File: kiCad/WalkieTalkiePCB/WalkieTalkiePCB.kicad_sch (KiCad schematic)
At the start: 21 parts, among them SW1 UP, SW2 DWN, SW3 MODE, SW4 TLK, SW5 XTRA, U1 I2S-MIC, U2 3006-ADA_Adafruit_, U3 WROOM-32_DEVKITV1, U4 OLED_DISPLAY, U5 BAT-C-10TYPEC, U6 PSM-301, U7 PBS-LED-1606WH-L

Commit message: Kicad Finalized Schematic
Colin Jack is smort
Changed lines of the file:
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@@
   (junction (at 120.65 54.61) (diameter 0) (color 0 0 0 0)
-  )
-  (junction (at 87.63 87.63) (diameter 0) (color 0 0 0 0)
   )
   (junction (at 120.65 68.58) (diameter 0) (color 0 0 0 0)
@@
     (stroke (width 0) (type default) (color 0 0 0 0))
   )
-  (wire (pts (xy 87.63 87.63) (xy 87.63 107.95))
-    (stroke (width 0) (type default) (color 0 0 0 0))
-  )
   (wire (pts (xy 64.77 124.46) (xy 86.36 124.46))
     (stroke (width 0) (type default) (color 0 0 0 0))
@@
     (stroke (width 0) (type default) (color 0 0 0 0))
   )
-  (wire (pts (xy 87.63 87.63) (xy 97.79 87.63))
-    (stroke (width 0) (type default) (color 0 0 0 0))
-  )
   (wire (pts (xy 217.17 124.46) (xy 217.17 133.35))
     (stroke (width 0) (type default) (color 0 0 0 0))
@@
     (stroke (width 0) (type default) (color 0 0 0 0))
   )
-  (wire (pts (xy 87.63 107.95) (xy 113.03 107.95))
-    (stroke (width 0) (type default) (color 0 0 0 0))
-  )
   (wire (pts (xy 210.82 107.95) (xy 210.82 121.92))
     (stroke (width 0) (type default) (color 0 0 0 0))
@@
     (stroke (width 0) (type default) (color 0 0 0 0))
   )
-  (wire (pts (xy 86.36 87.63) (xy 87.63 87.63))
+  (wire (pts (xy 86.36 87.63) (xy 97.79 87.63))
     (stroke (width 0) (type default) (color 0 0 0 0))
   )
@@
     (pin "1")
   )
-  (symbol (lib_id "power:PWR_FLAG") (at 30.48 19.05 180) (unit 1)
-    (in_bom yes) (on_board yes) (fields_autoplaced)
-    (property "Reference" "#FLG0102" (id 0) (at 30.48 20.955 0)
-      (effects (font (size 1.27 1.27)) hide)
-    )
-    (property "Value" "PWR_FLAG" (id 1) (at 30.48 24.13 0))
-    (property "Footprint" "" (id 2) (at 30.48 19.05 0)
-      (effects (font (size 1.27 1.27)) hide)
-    )
-    (property "Datasheet" "~" (id 3) (at 30.48 19.05 0)
-      (effects (font (size 1.27 1.27)) hide)
-    )
-    (pin "1")
-  )
   (symbol (lib_id "power:VCC") (at 264.16 93.98 0) (unit 1)
     (in_bom yes) (on_board yes) (fields_autoplaced)
@@
     (pin "2")
   )
-  (symbol (lib_id "power:VCC") (at 20.32 19.05 0) (unit 1)
-    (in_bom yes) (on_board yes) (fields_autoplaced)
-    (property "Reference" "#PWR0102" (id 0) (at 20.32 22.86 0)
-      (effects (font (size 1.27 1.27)) hide)
-    )
-    (property "Value" "VCC" (id 1) (at 20.32 13.97 0))
-    (property "Footprint" "" (id 2) (at 20.32 19.05 0)
-      (effects (font (size 1.27 1.27)) hide)
-    )
-    (property "Datasheet" "" (id 3) (at 20.32 19.05 0)
-      (effects (font (size 1.27 1.27)) hide)
-    )
-    (pin "1")
-  )
   (symbol (lib_id "Device:R") (at 199.39 116.84 0) (unit 1)
     (in_bom yes) (on_board yes) (fields_autoplaced)
@@
     (pin "1")
     (pin "2")
-  )
-  (symbol (lib_id "power:GND") (at 30.48 19.05 180) (unit 1)
-    (in_bom yes) (on_board yes) (fields_autoplaced)
-    (property "Reference" "#PWR0101" (id 0) (at 30.48 12.7 0)
-      (effects (font (size 1.27 1.27)) hide)
-    )
-    (property "Value" "GND" (id 1) (at 30.48 13.97 0))
-    (property "Footprint" "" (id 2) (at 30.48 19.05 0)
-      (effects (font (size 1.27 1.27)) hide)
-    )
-    (property "Datasheet" "" (id 3) (at 30.48 19.05 0)
-      (effects (font (size 1.27 1.27)) hide)
-    )
-    (pin "1")
   )
   (symbol (lib_id "Device:Speaker") (at 121.92 157.48 270) (unit 1)
@@
     (pin "2")
   )
-  (symbol (lib_id "power:PWR_FLAG") (at 20.32 19.05 180) (unit 1)
-    (in_bom yes) (on_board yes) (fields_autoplaced)
-    (property "Reference" "#FLG0103" (id 0) (at 20.32 20.955 0)
-      (effects (font (size 1.27 1.27)) hide)
-    )
-    (property "Value" "PWR_FLAG" (id 1) (at 20.32 24.13 0))
-    (property "Footprint" "" (id 2) (at 20.32 19.05 0)
-      (effects (font (size 1.27 1.27)) hide)
-    )
-    (property "Datasheet" "~" (id 3) (at 20.32 19.05 0)
-      (effects (font (size 1.27 1.27)) hide)
-    )
-    (pin "1")
-  )
   (symbol (lib_id "power:VCC") (at 158.75 127 180) (unit 1)
     (in_bom yes) (on_board yes) (fields_autoplaced)
@@
       (reference "#FLG0101") (unit 1) (value "PWR_FLAG") (footprint "")
     )
-    (path "/11edab21-699f-42c5-8fca-4d804925d8d4"
-      (reference "#FLG0102") (unit 1) (value "PWR_FLAG") (footprint "")
-    )
-    (path "/f00c2272-6d64-46d9-8dbf-cbfe852eec09"
-      (reference "#FLG0103") (unit 1) (value "PWR_FLAG") (footprint "")
-    )
     (path "/dde1a039-bfd3-47af-b1ef-c50a0b5b415b"
       (reference "#FLG0104") (unit 1) (value "PWR_FLAG") (footprint "")
     )
-    (path "/6ede4dce-002e-42b0-be72-ae433793c82f"
-      (reference "#PWR0101") (unit 1) (value "GND") (footprint "")
-    )
-    (path "/1ae2b874-5753-46d5-b3c2-00fc7ac6cbb4"
-      (reference "#PWR0102") (unit 1) (value "VCC") (footprint "")
-    )
     (path "/1229cc48-894a-4616-bade-a8d099b6e899"

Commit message: PCB
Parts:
- BT1: footprint (none) -> ESP32 Walkie-Talkie:Battery-Contacts
- LS1: footprint (none) -> ESP32 Walkie-Talkie:Speaker
- U1: footprint (none) -> ESP32 Walkie-Talkie:I2S-Mic
- U2: footprint (none) -> ESP32 Walkie-Talkie:Amplifier
- U5: footprint (none) -> ESP32 Walkie-Talkie:USBC-BMS
- U6: footprint (none) -> ESP32 Walkie-Talkie:Voltage-Regulator
- U7: footprint (none) -> ESP32 Walkie-Talkie:PBS-Button
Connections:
- net at U6.VIN+: now also U5.V+ (VOUT); no longer U5.v+ (VOUT)
- net at U6.VIN-: now also U5.V- (VOUT); no longer U5.v- (VOUT)
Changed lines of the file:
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@@
     (property "Reference" "U1" (id 0) (at 71.12 125.73 0))
     (property "Value" "I2S-MIC" (id 1) (at 71.12 128.27 0))
-    (property "Footprint" "" (id 2) (at 71.12 139.7 0)
+    (property "Footprint" "ESP32 Walkie-Talkie:I2S-Mic" (id 2) (at 71.12 139.7 0)
       (effects (font (size 1.27 1.27)) hide)
     )
@@
       (effects (font (size 1.27 1.27)) (justify left))
     )
-    (property "Footprint" "" (id 2) (at 125.73 125.73 0)
+    (property "Footprint" "ESP32 Walkie-Talkie:Amplifier" (id 2) (at 125.73 125.73 0)
       (effects (font (size 1.27 1.27)) hide)
     )
@@
     (property "Reference" "BT1" (id 0) (at 214.122 127 90))
     (property "Value" "Battery_Cell" (id 1) (at 214.122 129.54 90))
-    (property "Footprint" "" (id 2) (at 213.614 134.62 90)
+    (property "Footprint" "ESP32 Walkie-Talkie:Battery-Contacts" (id 2) (at 213.614 134.62 90)
       (effects (font (size 1.27 1.27)) hide)
     )
@@
       (effects (font (size 1.27 1.27)) (justify left))
     )
-    (property "Footprint" "" (id 2) (at 116.84 157.48 0)
+    (property "Footprint" "ESP32 Walkie-Talkie:Speaker" (id 2) (at 116.84 157.48 0)
       (effects (font (size 1.27 1.27)) hide)
     )
@@
       (effects (font (size 1.27 1.27)) (justify left))
     )
-    (property "Footprint" "" (id 2) (at 213.36 88.9 0)
+    (property "Footprint" "ESP32 Walkie-Talkie:USBC-BMS" (id 2) (at 213.36 88.9 0)
       (effects (font (size 1.27 1.27)) hide)
     )
@@
     (pin "B+")
     (pin "B-")
-    (pin "v+")
-    (pin "v-")
+    (pin "V+")
+    (pin "V-")
   )
   (symbol (lib_id "WalkieTalkie:PSM-301") (at 214.63 91.44 180) (unit 1)
@@
     (property "Reference" "U6" (id 0) (at 213.995 88.9 0))
     (property "Value" "PSM-301" (id 1) (at 213.995 91.44 0))
-    (property "Footprint" "" (id 2) (at 214.63 91.44 0)
+    (property "Footprint" "ESP32 Walkie-Talkie:Voltage-Regulator" (id 2) (at 214.63 91.44 0)
       (effects (font (size 1.27 1.27)) hide)
     )
@@
     (property "Reference" "U7" (id 0) (at 262.89 82.55 0))
     (property "Value" "PBS-LED-1606WH-L" (id 1) (at 262.89 85.09 0))
-    (property "Footprint" "" (id 2) (at 251.46 87.63 0)
+    (property "Footprint" "ESP32 Walkie-Talkie:PBS-Button" (id 2) (at 251.46 87.63 0)
       (effects (font (size 1.27 1.27)) hide)
     )
@@
     )
     (path "/565d06fb-9534-48e0-a256-9134feb87b03"
-      (reference "BT1") (unit 1) (value "Battery_Cell") (footprint "")
+      (reference "BT1") (unit 1) (value "Battery_Cell") (footprint "ESP32 Walkie-Talkie:Battery-Contacts")
     )
     (path "/729b3da4-0313-41c5-9118-f5a5d81e720a"
-      (reference "LS1") (unit 1) (value "Speaker") (footprint "")
+      (reference "LS1") (unit 1) (value "Speaker") (footprint "ESP32 Walkie-Talkie:Speaker")
     )
     (path "/e9eb94ed-4dc4-450e-8838-fce3918021eb"
@@
     )
     (path "/06189962-e377-4982-9780-d7fd696848a8"
-      (reference "U1") (unit 1) (value "I2S-MIC") (footprint "")
+      (reference "U1") (unit 1) (value "I2S-MIC") (footprint "ESP32 Walkie-Talkie:I2S-Mic")
     )
     (path "/0aeafca2-1eb3-4ed4-9136-be9da76bceb3"
-      (reference "U2") (unit 1) (value "3006-ADA_Adafruit_") (footprint "")
+      (reference "U2") (unit 1) (value "3006-ADA_Adafruit_") (footprint "ESP32 Walkie-Talkie:Amplifier")
     )
     (path "/c943f0b5-36cc-4140-b0cd-7d88893d98d2"
@@
     )
     (path "/742e5744-c81c-4950-88db-007b37fa2b34"
-      (reference "U5") (unit 1) (value "BAT-C-10TYPEC") (footprint "")
+      (reference "U5") (unit 1) (value "BAT-C-10TYPEC") (footprint "ESP32 Walkie-Talkie:USBC-BMS")
     )
     (path "/75cb9de8-b81e-4952-a80b-0fda81fc1740"
-      (reference "U6") (unit 1) (value "PSM-301") (footprint "")
+      (reference "U6") (unit 1) (value "PSM-301") (footprint "ESP32 Walkie-Talkie:Voltage-Regulator")
     )
     (path "/906709c3-3cb2-4376-82e4-c4c35bb617e0"
-      (reference "U7") (unit 1) (value "PBS-LED-1606WH-L") (footprint "")
-    )
-  )
+      (reference "U7") (unit 1) (value "PBS-LED-1606WH-L") (footprint "ESP32 Walkie-Talkie:PBS-Button")
+    )
+  )

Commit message: PCB
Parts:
- removed U1: I2S-MIC, ESP32 Walkie-Talkie:I2S-Mic, symbol WalkieTalkie:I2S-MIC
- removed U2: 3006-ADA_Adafruit_, ESP32 Walkie-Talkie:Amplifier, symbol WalkieTalkie:3006-ADA_Adafruit_
- removed U3: WROOM-32_DEVKITV1, symbol WROOM32-DEVKITV1:WROOM-32_DEVKITV1
- removed U4: OLED_DISPLAY, symbol WalkieTalkie:OLED_DISPLAY
- removed U5: BAT-C-10TYPEC, ESP32 Walkie-Talkie:USBC-BMS, symbol WalkieTalkie:BAT-C-10TYPEC
- removed U6: PSM-301, ESP32 Walkie-Talkie:Voltage-Regulator, symbol WalkieTalkie:PSM-301
- removed U7: PBS-LED-1606WH-L, ESP32 Walkie-Talkie:PBS-Button, symbol WalkieTalkie:PBS-LED-1606WH-L
- added U1: BAT-C-10TYPEC_(BMS), ESP32-Walkie-Talkie-Footprints-Remaster:BAT-C-10TYPEC-BMS, symbol Walkie-Talkie-Symbols-Remastered:BAT-C-10TYPEC_(BMS)
- added U2: PSM-301-Voltage-Regulator, ESP32-Walkie-Talkie-Footprints-Remaster:PSM-301-Voltage-Regulator, symbol Walkie-Talkie-Symbols-Remastered:PSM-301-Voltage-Regulator
- added U3: PBS-LED-1606WH-L_(Toggle_Button), ESP32-Walkie-Talkie-Footprints-Remaster:PBS-LED-1606WH-L-Toggle-Switch, symbol Walkie-Talkie-Symbols-Remastered:PBS-LED-1606WH-L_(Toggle_Button)
- added U4: I2S-128X64-OLED-LCD_, ESP32-Walkie-Talkie-Footprints-Remaster:I2S-128x64-OLED-LCD, symbol Walkie-Talkie-Symbols-Remastered:I2S-128X64-OLED-LCD_
- added U5: I2S-INMP441_(MIC), ESP32-Walkie-Talkie-Footprints-Remaster:I2SINMP441-MIC, symbol Walkie-Talkie-Symbols-Remastered:I2S-INMP441_(MIC)
- added U6: Amplifier, ESP32-Walkie-Talkie-Footprints-Remaster:Amplifier, symbol Walkie-Talkie-Symbols-Remastered:Amplifier
- added U7: ESP-WROOM-32, esp32_devkit_v1_doit:esp32_devkit_v1_doit, symbol Walkie-Talkie-Symbols-Remastered:ESP-WROOM-32
- BT1: footprint ESP32 Walkie-Talkie:Battery-Contacts -> ESP32-Walkie-Talkie-Footprints-Remaster:BATTERY-CONTACTS
- LS1: footprint ESP32 Walkie-Talkie:Speaker -> ESP32-Walkie-Talkie-Footprints-Remaster:SPEAKER
- R1, R2, R3, R4, R5: footprint (none) -> Resistor_THT:R_Axial_DIN0207_L6.3mm_D2.5mm_P10.16mm_Horizontal
- R6: value 2k2 -> 2K; footprint (none) -> Resistor_THT:R_Axial_DIN0207_L6.3mm_D2.5mm_P10.16mm_Horizontal
- R7: value 2k -> 2K2; footprint (none) -> Resistor_THT:R_Axial_DIN0207_L6.3mm_D2.5mm_P10.16mm_Horizontal
- SW1, SW2, SW3, SW4, SW5: footprint (none) -> ESP32-Walkie-Talkie-Footprints-Remaster:PUSH-BUTTON-CONTACTS
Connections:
- net GND: now also U2.2 (VOUT-), U3.2 (-), U4.2 (GND), U5.3 (L/R), U5.6 (GND), U6.4 (GAIN), U6.6 (GND)
- net VCC: now also U2.1 (VOUT+), U3.1 (+), U4.1 (VCC), U5.5 (VDD), U6.7 (VIN)
- net at LS1.1: now also U6.8 (-)
- net at LS1.2: now also U6.9 (+)
- net at R4.2, SW4.2: now also U7.10 (D27)
- net at R3.2, SW3.2: now also U7.9 (D26)
- net at R6.2, R7.1: now also U7.4 (D34)
- net at BT1.1 (+), R7.2: now also U1.2 (B+), U3.3 (CC)
- net at R1.2, SW1.2: now also U7.23 (D5)
- net at R2.2, SW2.2: now also U7.21 (D19)
- net at BT1.2 (-): now also U1.3 (B-)
- net at R5.2, SW5.2: now also U7.5 (D35)
- new net: U5.1 (SCK), U6.2 (BLCK), U7.6 (D32)
- new net: U5.2 (WS), U6.1 (LRC), U7.8 (D25)
- new net: U5.4 (SD), U7.7 (D33)
- new net: U2.5 (EN), U3.4 (NO)
- new net: U1.1 (OUT+), U2.4 (VIN+)
- new net: U1.4 (OUT-), U2.3 (VIN-)
- new net: U6.3 (DIN), U7.11 (D14)
- new net: U4.3 (SCL), U7.17 (D22)
- new net: U4.4 (SDA), U7.20 (D21)
- no-connect marks 20 -> 22
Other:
- note added: "Interact"
- note removed: "DISPLAY"
- note removed: "Input System"
- note removed: "Power Management"
- moved on the sheet: R1, R2, R3, R4, R5, SW1, SW2, SW3, SW4, SW5

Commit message: PCB
Why do we live. Just to suffer.
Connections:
- net GND: now also U7.29 (GND)
- net VCC: now also U7.30 (3V3)
- no-connect marks 22 -> 20
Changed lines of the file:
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@@
   (no_connect (at 207.01 87.63))
   (no_connect (at 165.1 96.52))
-  (no_connect (at 165.1 109.22))
   (no_connect (at 139.7 106.68))
   (no_connect (at 165.1 83.82))
@@
   (no_connect (at 139.7 78.74))
   (no_connect (at 165.1 76.2))
-  (no_connect (at 165.1 111.76))
   (no_connect (at 139.7 111.76))
   (no_connect (at 165.1 99.06))
@@
     (stroke (width 0) (type default) (color 0 0 0 0))
   )
+  (wire (pts (xy 165.1 111.76) (xy 165.1 115.57))
+    (stroke (width 0) (type default) (color 0 0 0 0))
+  )
   (wire (pts (xy 212.09 114.3) (xy 212.09 85.09))
     (stroke (width 0) (type default) (color 0 0 0 0))
@@
     (stroke (width 0) (type default) (color 0 0 0 0))
   )
+  (wire (pts (xy 168.91 109.22) (xy 168.91 113.03))
+    (stroke (width 0) (type default) (color 0 0 0 0))
+  )
   (wire (pts (xy 134.62 123.19) (xy 134.62 128.27))
     (stroke (width 0) (type default) (color 0 0 0 0))
@@
   )
   (wire (pts (xy 91.44 147.32) (xy 91.44 148.59))
+    (stroke (width 0) (type default) (color 0 0 0 0))
+  )
+  (wire (pts (xy 165.1 109.22) (xy 168.91 109.22))
     (stroke (width 0) (type default) (color 0 0 0 0))
   )
@@
     (pin "1")
     (pin "2")
+  )
+  (symbol (lib_id "power:GND") (at 168.91 113.03 0) (unit 1)
+    (in_bom yes) (on_board yes) (fields_autoplaced)
+    (property "Reference" "#PWR011" (id 0) (at 168.91 119.38 0)
+      (effects (font (size 1.27 1.27)) hide)
+    )
+    (property "Value" "GND" (id 1) (at 168.91 118.11 0))
+    (property "Footprint" "" (id 2) (at 168.91 113.03 0)
+      (effects (font (size 1.27 1.27)) hide)
+    )
+    (property "Datasheet" "" (id 3) (at 168.91 113.03 0)
+      (effects (font (size 1.27 1.27)) hide)
+    )
+    (pin "1")
   )
   (symbol (lib_id "Switch:SW_Push") (at 83.82 76.2 90) (unit 1)
@@
     (pin "4")
     (pin "5")
+  )
+  (symbol (lib_id "power:VCC") (at 165.1 115.57 180) (unit 1)
+    (in_bom yes) (on_board yes) (fields_autoplaced)
+    (property "Reference" "#PWR010" (id 0) (at 165.1 111.76 0)
+      (effects (font (size 1.27 1.27)) hide)
+    )
+    (property "Value" "VCC" (id 1) (at 165.1 120.65 0))
+    (property "Footprint" "" (id 2) (at 165.1 115.57 0)
+      (effects (font (size 1.27 1.27)) hide)
+    )
+    (property "Datasheet" "" (id 3) (at 165.1 115.57 0)
+      (effects (font (size 1.27 1.27)) hide)
+    )
+    (pin "1")
   )
   (symbol (lib_id "Walkie-Talkie-Symbols-Remastered:BAT-C-10TYPEC_(BMS)") (at 203.2 97.79 180) (unit 1)
@@
       (reference "#PWR09") (unit 1) (value "VCC") (footprint "")
     )
+    (path "/91b2fa62-6d51-424a-b6bc-28f3d4391629"
+      (reference "#PWR010") (unit 1) (value "VCC") (footprint "")
+    )
+    (path "/4c787647-1296-428b-8dc3-b9558523d840"
+      (reference "#PWR011") (unit 1) (value "GND") (footprint "")
+    )
     (path "/52a0511d-0ae3-46a1-aba7-f13cd3fb2bd9"

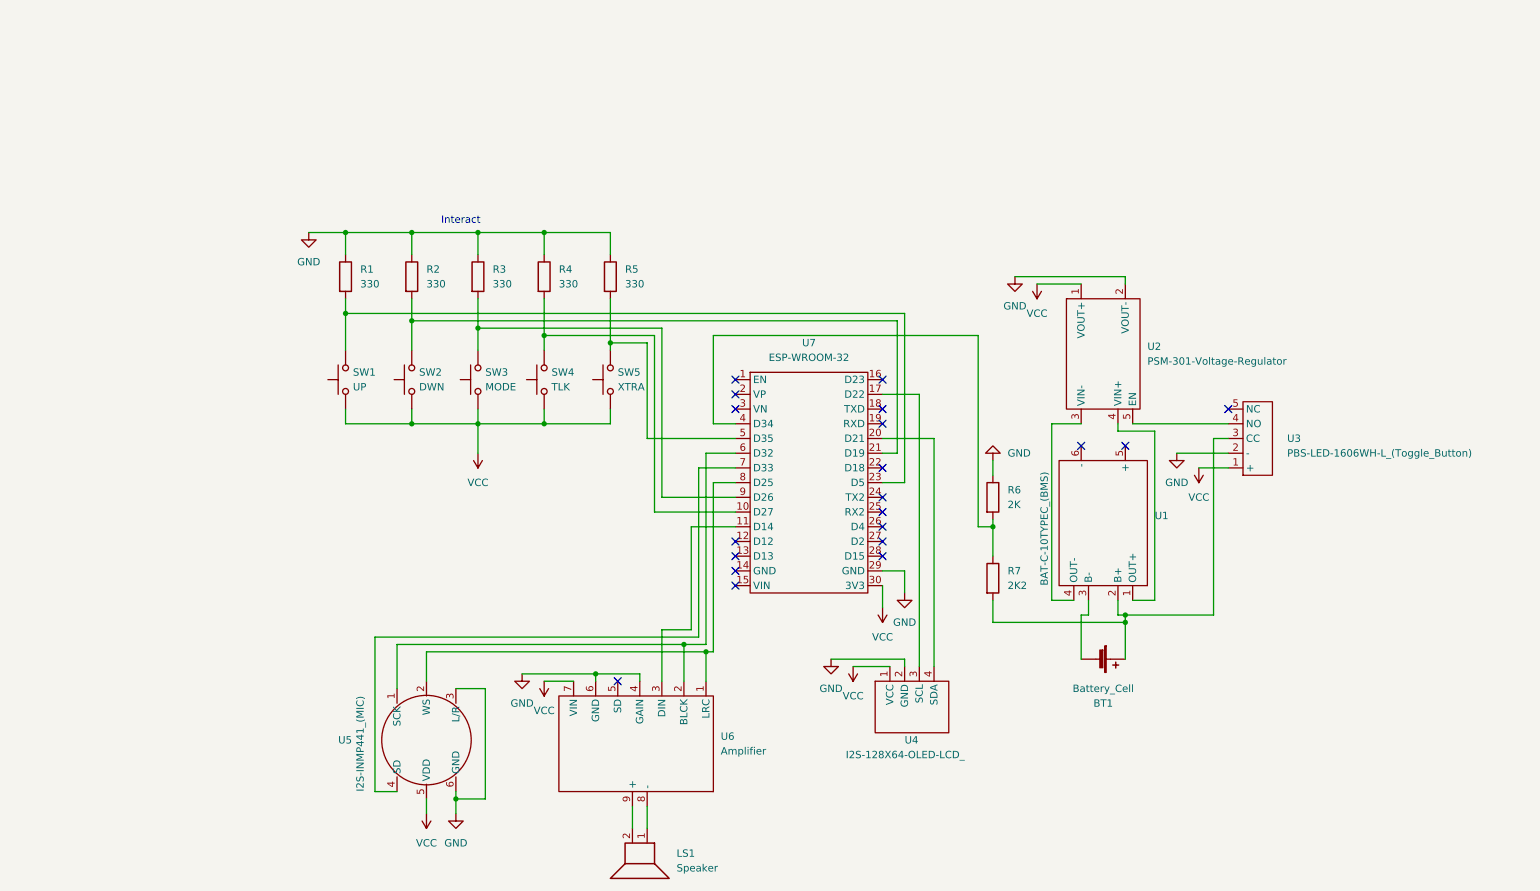
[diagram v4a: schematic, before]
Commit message: Final Route of PCB
- Generated JLC gerber
- Created BOM
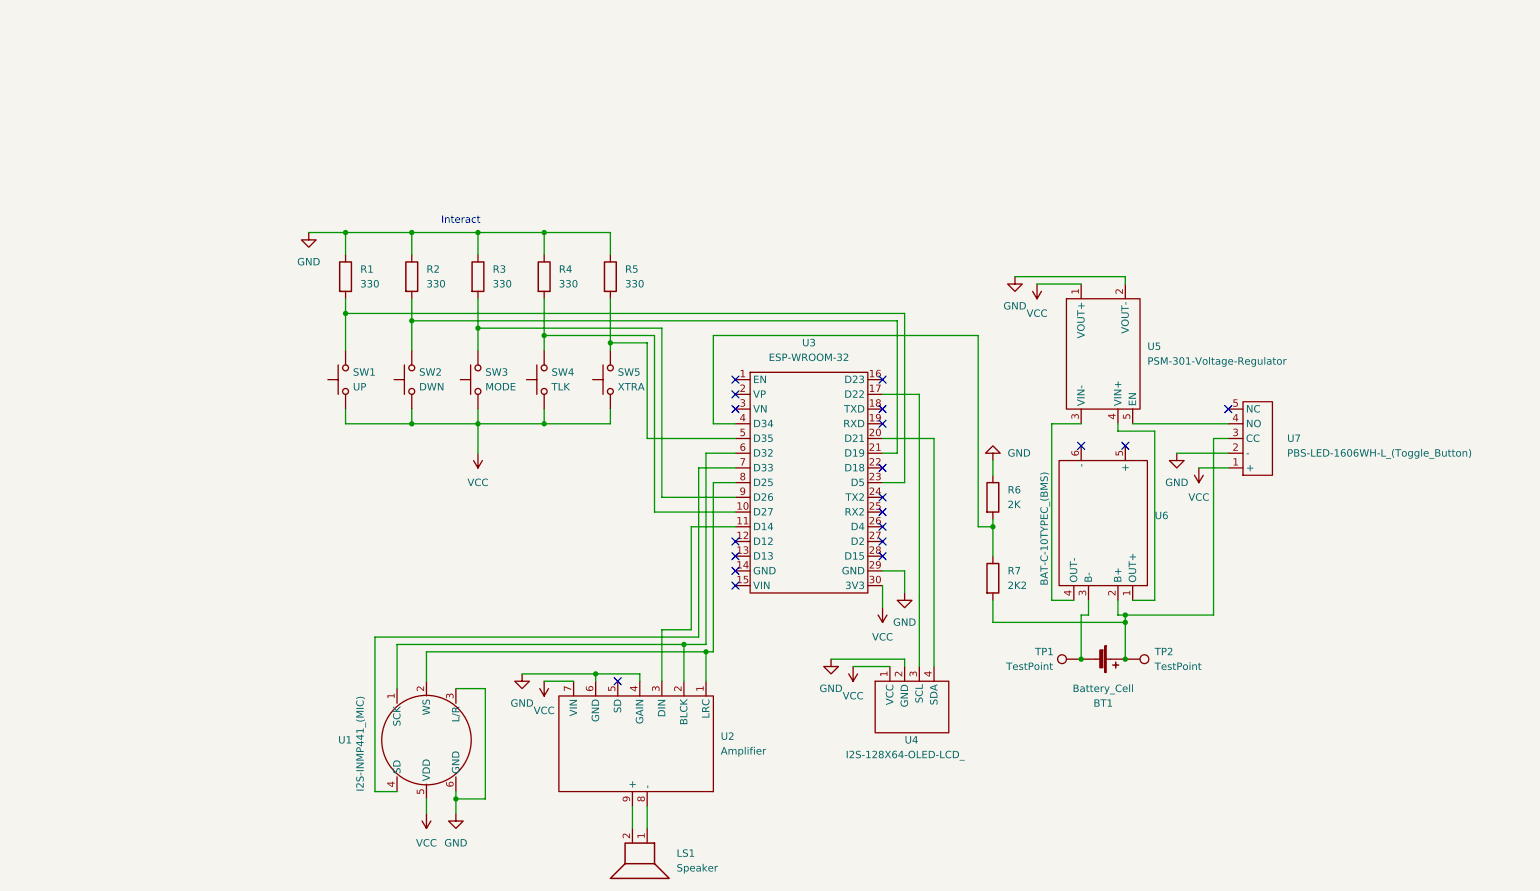
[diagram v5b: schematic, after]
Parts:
- added TP1, TP2: TestPoint, symbol Connector:TestPoint
- renumbered U5 to U1, U6 to U2, U7 to U3, U2 to U5, U1 to U6, U3 to U7
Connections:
- net at BT1.1 (+), R7.2, U6.2 (B+)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: now also TP2.1
- net at BT1.2 (-), U6.3 (B-): now also TP1.1
